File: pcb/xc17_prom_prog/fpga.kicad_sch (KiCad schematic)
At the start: 18 parts, among them J3 Conn_02x20_Odd_Even, U3 ICE40HX1K-VQ100

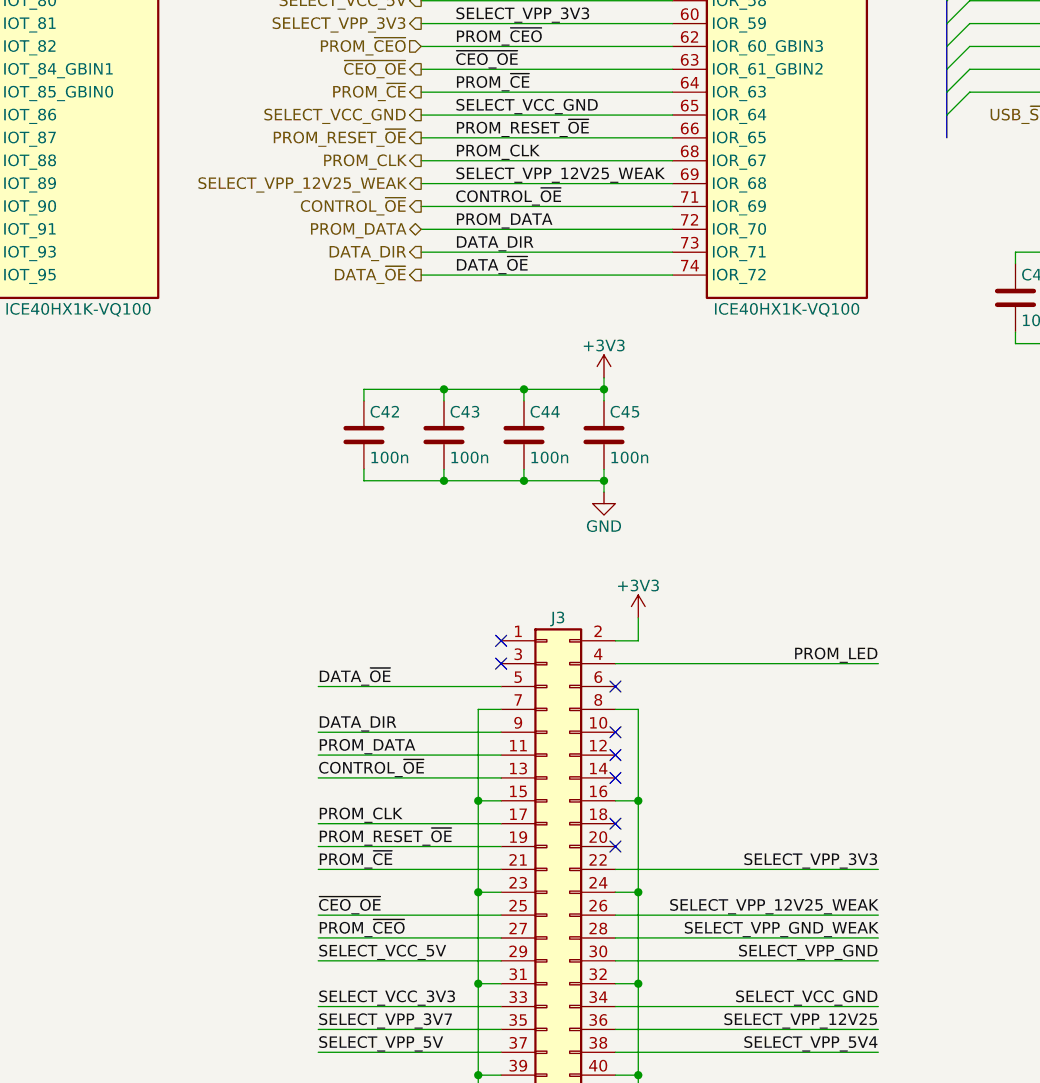
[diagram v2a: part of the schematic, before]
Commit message: Remove unused components
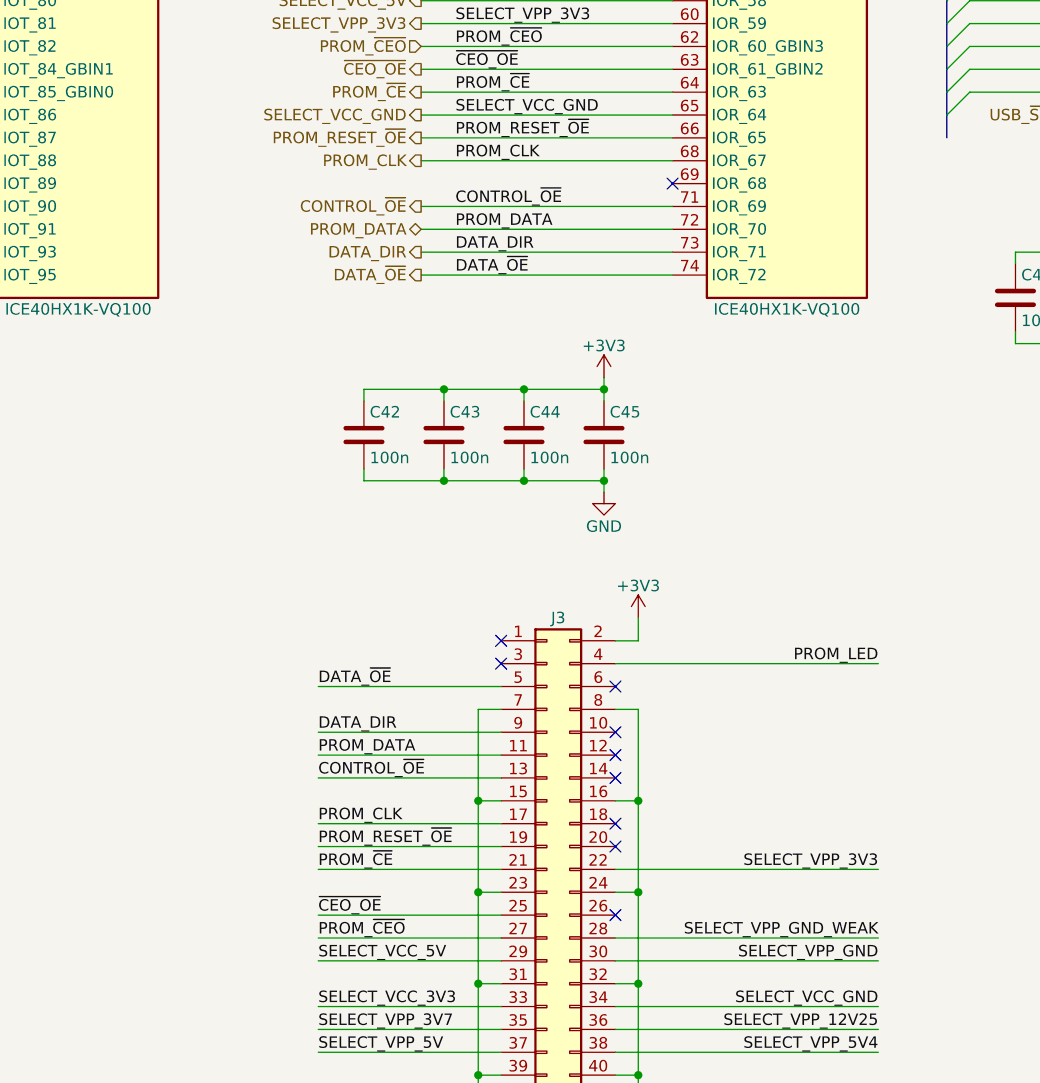
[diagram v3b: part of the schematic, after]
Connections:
- net SELECT_VPP_12V25_WEAK: no longer names the net of U3.69 (IOR_68)
- net SELECT_VPP_12V25_WEAK: no longer J3.26 (Pin_26)
- no-connect marks 39 -> 41
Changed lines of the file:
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@@
 	(title_block
 		(title "XC17xxx PROM Programmer")
-		(date "2024-12-08")
-		(rev "2")
+		(date "2025-01-29")
+		(rev "3")
 		(company "CC-BY-SA-4.0 Michael Singer")
 		(comment 1 "https://github.com/msinger/xc17_prom_prog/")
@@
 	)
 	(no_connect
+		(at 144.78 157.48)
+	)
+	(no_connect
 		(at 144.78 137.16)
 	)
@@
 	(no_connect
 		(at 257.81 55.88)
+	)
+	(no_connect
+		(at 151.13 76.2)
 	)
 	(no_connect
@@
 	(wire
 		(pts
-			(xy 123.19 76.2) (xy 151.13 76.2)
-		)
-		(stroke
-			(width 0)
-			(type default)
-		)
-	)
-	(wire
-		(pts
 			(xy 43.18 86.36) (xy 72.39 86.36)
 		)
@@
 		(pts
 			(xy 123.19 40.64) (xy 151.13 40.64)
-		)
-		(stroke
-			(width 0)
-			(type default)
-		)
-	)
-	(wire
-		(pts
-			(xy 144.78 157.48) (xy 173.99 157.48)
 		)
 		(stroke
@@
 		)
 	)
-	(label "SELECT_VPP_12V25_WEAK"
-		(at 127 76.2 0)
-		(fields_autoplaced yes)
-		(effects
-			(font
-				(size 1.27 1.27)
-			)
-			(justify left bottom)
-		)
-	)
 	(label "PROM_CLK"
 		(at 111.76 147.32 0)
@@
 			)
 			(justify left bottom)
-		)
-	)
-	(label "SELECT_VPP_12V25_WEAK"
-		(at 173.99 157.48 180)
-		(fields_autoplaced yes)
-		(effects
-			(font
-				(size 1.27 1.27)
-			)
-			(justify right bottom)
 		)
 	)
@@
 		(fields_autoplaced yes)
 		(effects
-			(font
-				(size 1.27 1.27)
-			)
-			(justify right)
-		)
-	)
-	(hierarchical_label "SELECT_VPP_12V25_WEAK"
-		(shape output)
-		(at 123.19 76.2 180)
-		(fields_autoplaced yes)
-		(effects

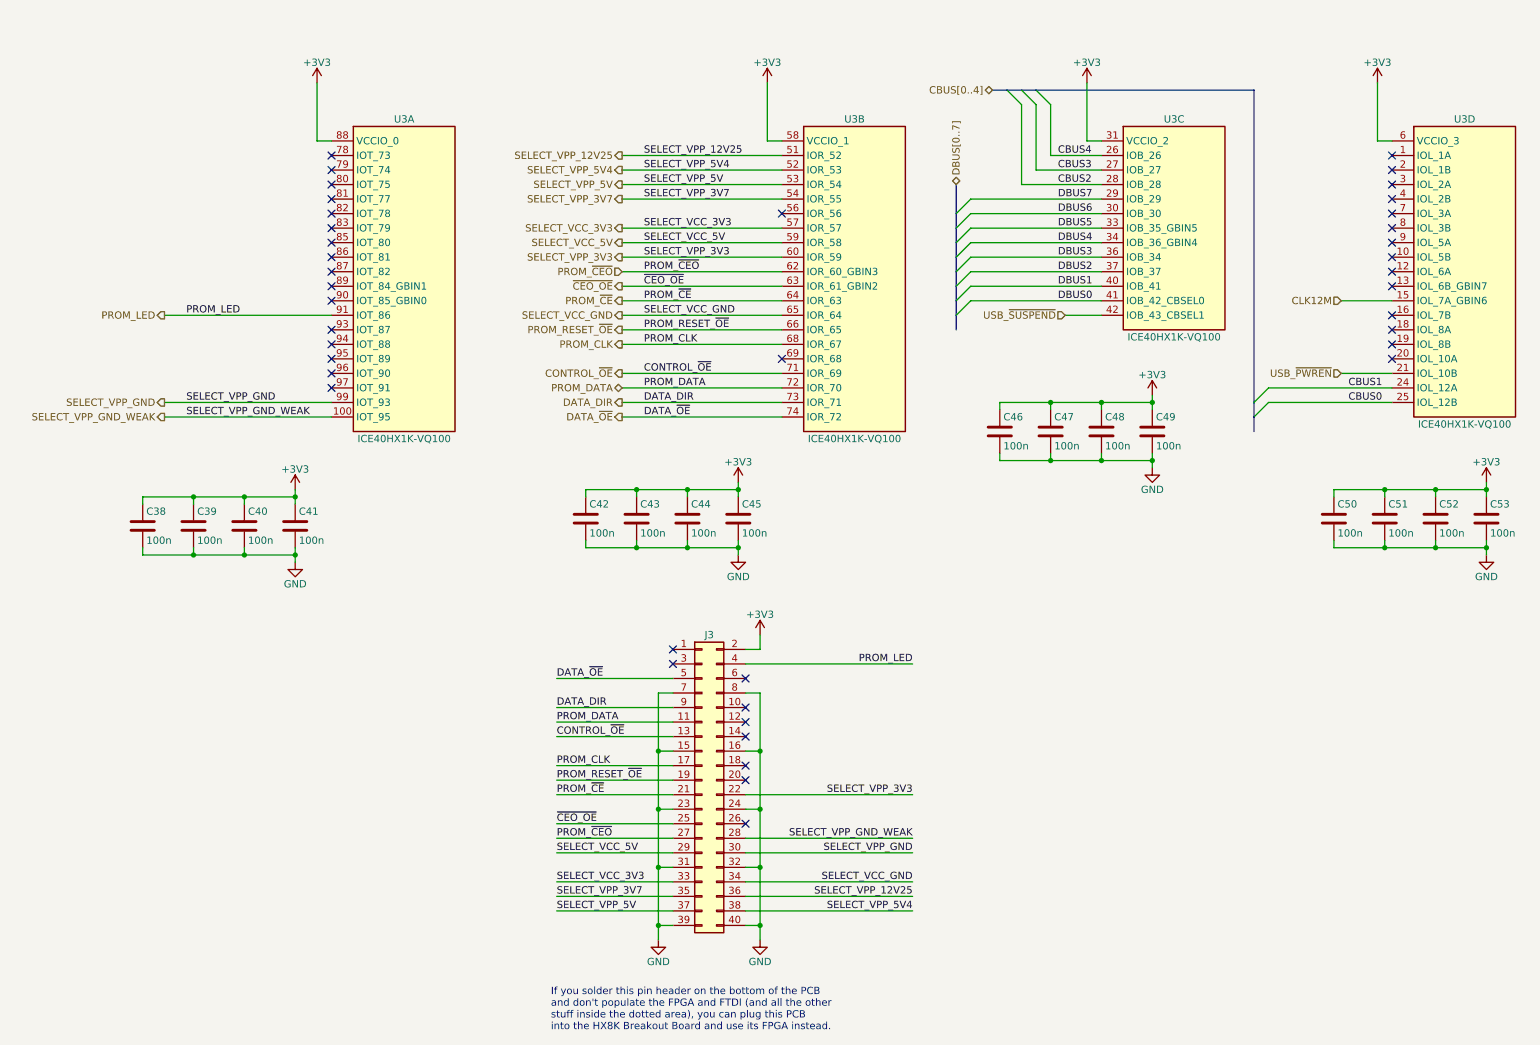
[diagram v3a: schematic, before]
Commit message: Migrate from HX1K to HX4K FPGA
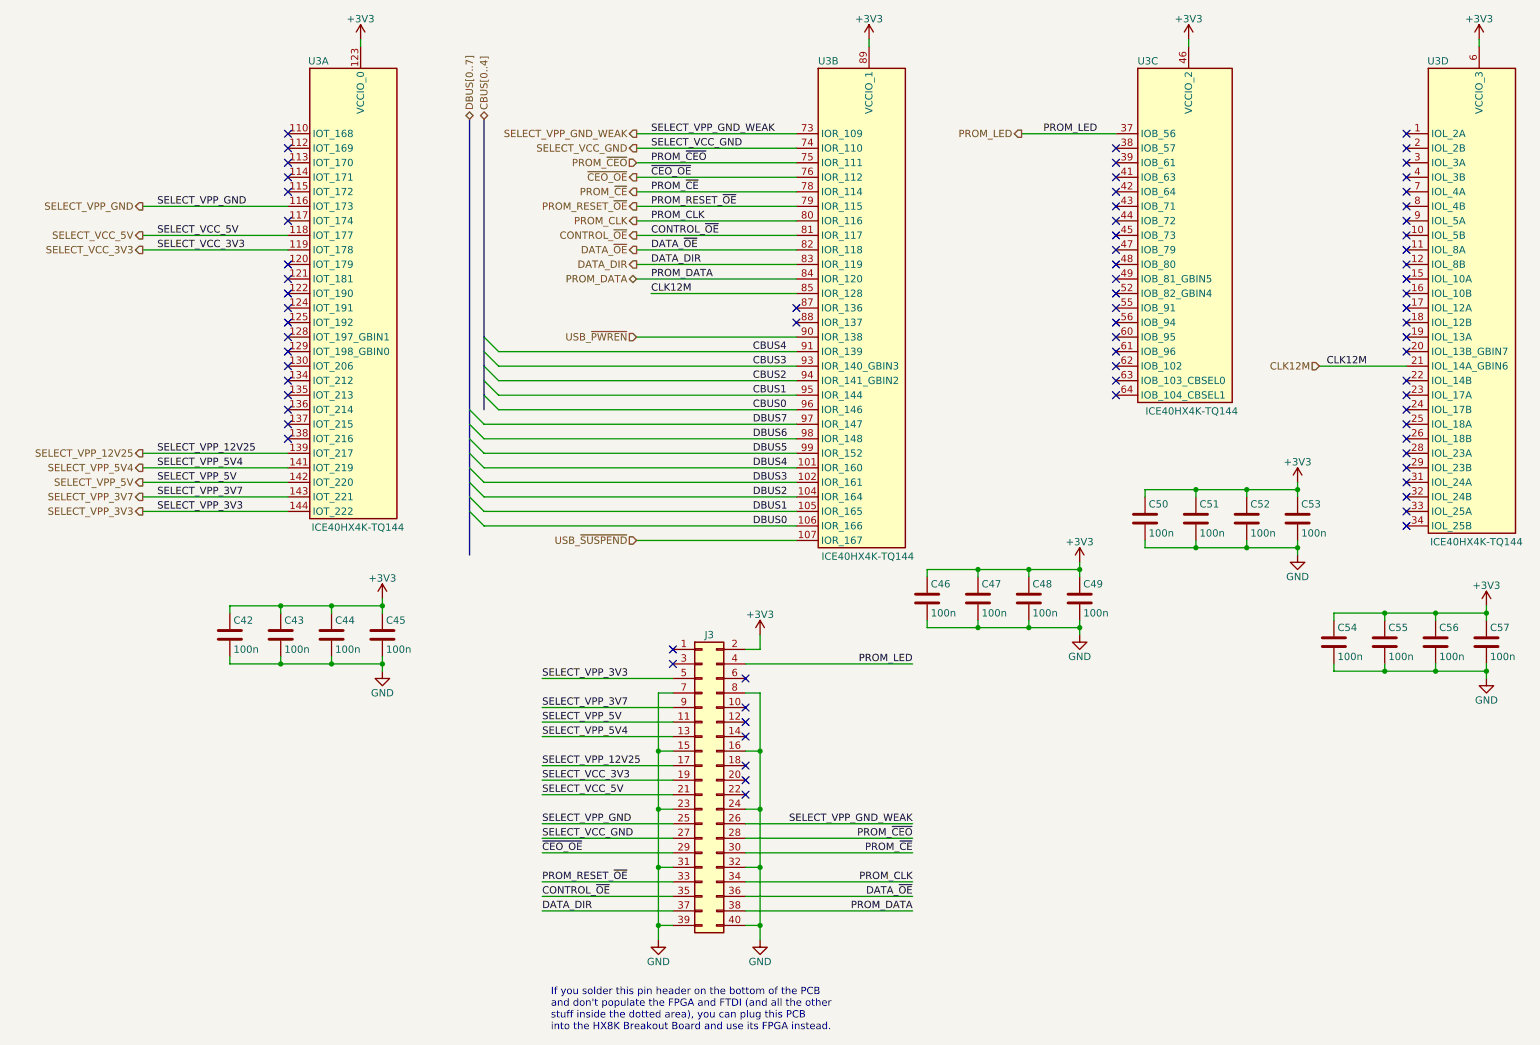
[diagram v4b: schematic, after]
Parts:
- removed U3: ICE40HX1K-VQ100, Package_QFP:VQFP-100_14x14mm_P0.5mm, symbol FPGA_Lattice_ICE40HX1K:ICE40HX1K-VQ100
- added U3: ICE40HX4K-TQ144, Package_QFP:TQFP-144_20x20mm_P0.5mm, symbol FPGA_Lattice:ICE40HX4K-TQ144
- renumbered C38 to C42, C39 to C43, C40 to C44, C41 to C45, C42 to C46, C43 to C47, C44 to C48, C45 to C49, C46 to C50, C47 to C51, C48 to C52, C49 to C53, C50 to C54, C51 to C55, C52 to C56, C53 to C57
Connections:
- net +3V3: now also U3.100 (VCCIO_1), U3.123 (VCCIO_0), U3.131 (VCCIO_0), U3.30 (VCCIO_3), U3.46 (VCCIO_2), U3.57 (VCCIO_2), U3.6 (VCCIO_3), U3.89 (VCCIO_1)
- net CBUS0: now also U3.96 (IOR_146)
- net CBUS1: now also U3.95 (IOR_144)
- net CBUS2: now also U3.94 (IOR_141_GBIN2)
- net CBUS3: now also U3.93 (IOR_140_GBIN3)
- net CBUS4: now also U3.91 (IOR_139)
- net CLK12M: now also U3.21 (IOL_14A_GBIN6), U3.85 (IOR_128)
- net CONTROL_~{OE}: now also J3.35 (Pin_35), U3.81 (IOR_117); no longer J3.13 (Pin_13)
- net DATA_DIR: now also J3.37 (Pin_37), U3.83 (IOR_119); no longer J3.9 (Pin_9)
- net DATA_~{OE}: now also J3.36 (Pin_36), U3.82 (IOR_118); no longer J3.5 (Pin_5)
- net DBUS0: now also U3.106 (IOR_166)
- net DBUS1: now also U3.105 (IOR_165)
- net DBUS2: now also U3.104 (IOR_164)
- net DBUS3: now also U3.102 (IOR_161)
- net DBUS4: now also U3.101 (IOR_160)
- net DBUS5: now also U3.99 (IOR_152)
- net DBUS6: now also U3.98 (IOR_148)
- net DBUS7: now also U3.97 (IOR_147)
- net PROM_CLK: now also J3.34 (Pin_34), U3.80 (IOR_116); no longer J3.17 (Pin_17)
- net PROM_DATA: now also J3.38 (Pin_38), U3.84 (IOR_120); no longer J3.11 (Pin_11)
- net PROM_LED: now also U3.37 (IOB_56)
- net PROM_RESET_~{OE}: now also J3.33 (Pin_33), U3.79 (IOR_115); no longer J3.19 (Pin_19)
- net PROM_~{CEO}: now also J3.28 (Pin_28), U3.75 (IOR_111); no longer J3.27 (Pin_27)
- net PROM_~{CE}: now also J3.30 (Pin_30), U3.78 (IOR_114); no longer J3.21 (Pin_21)
- net SELECT_VCC_3V3: now also J3.19 (Pin_19), U3.119 (IOT_178); no longer J3.33 (Pin_33)
- net SELECT_VCC_5V: now also J3.21 (Pin_21), U3.118 (IOT_177); no longer J3.29 (Pin_29)
- net SELECT_VCC_GND: now also J3.27 (Pin_27), U3.74 (IOR_110); no longer J3.34 (Pin_34)
- net SELECT_VPP_12V25: now also J3.17 (Pin_17), U3.139 (IOT_217); no longer J3.36 (Pin_36)
- net SELECT_VPP_3V3: now also J3.5 (Pin_5), U3.144 (IOT_222); no longer J3.22 (Pin_22)
- net SELECT_VPP_3V7: now also J3.9 (Pin_9), U3.143 (IOT_221); no longer J3.35 (Pin_35)
- net SELECT_VPP_5V: now also J3.11 (Pin_11), U3.142 (IOT_220); no longer J3.37 (Pin_37)
- net SELECT_VPP_5V4: now also J3.13 (Pin_13), U3.141 (IOT_219); no longer J3.38 (Pin_38)
- net SELECT_VPP_GND: now also J3.25 (Pin_25), U3.116 (IOT_173); no longer J3.30 (Pin_30)
- net SELECT_VPP_GND_WEAK: now also J3.26 (Pin_26), U3.73 (IOR_109); no longer J3.28 (Pin_28)
- net USB_~{PWREN}: now also U3.90 (IOR_138)
- net USB_~{SUSPEND}: now also U3.107 (IOR_167)
- net ~{CEO_OE}: now also J3.29 (Pin_29), U3.76 (IOR_112); no longer J3.25 (Pin_25)
- no-connect marks 41 -> 75
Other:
- moved on the sheet: C42, C43, C44, C45, C46, C47, C48, C49, C50, C51, C52, C53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
